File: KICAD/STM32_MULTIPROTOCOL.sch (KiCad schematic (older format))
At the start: 77 parts, among them T1 TestPoint, T10 TestPoint, T11 TestPoint, T12 TestPoint, T13 TestPoint, T14 TestPoint, T2 TestPoint, T3 TestPoint, T4 TestPoint, T5 TestPoint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

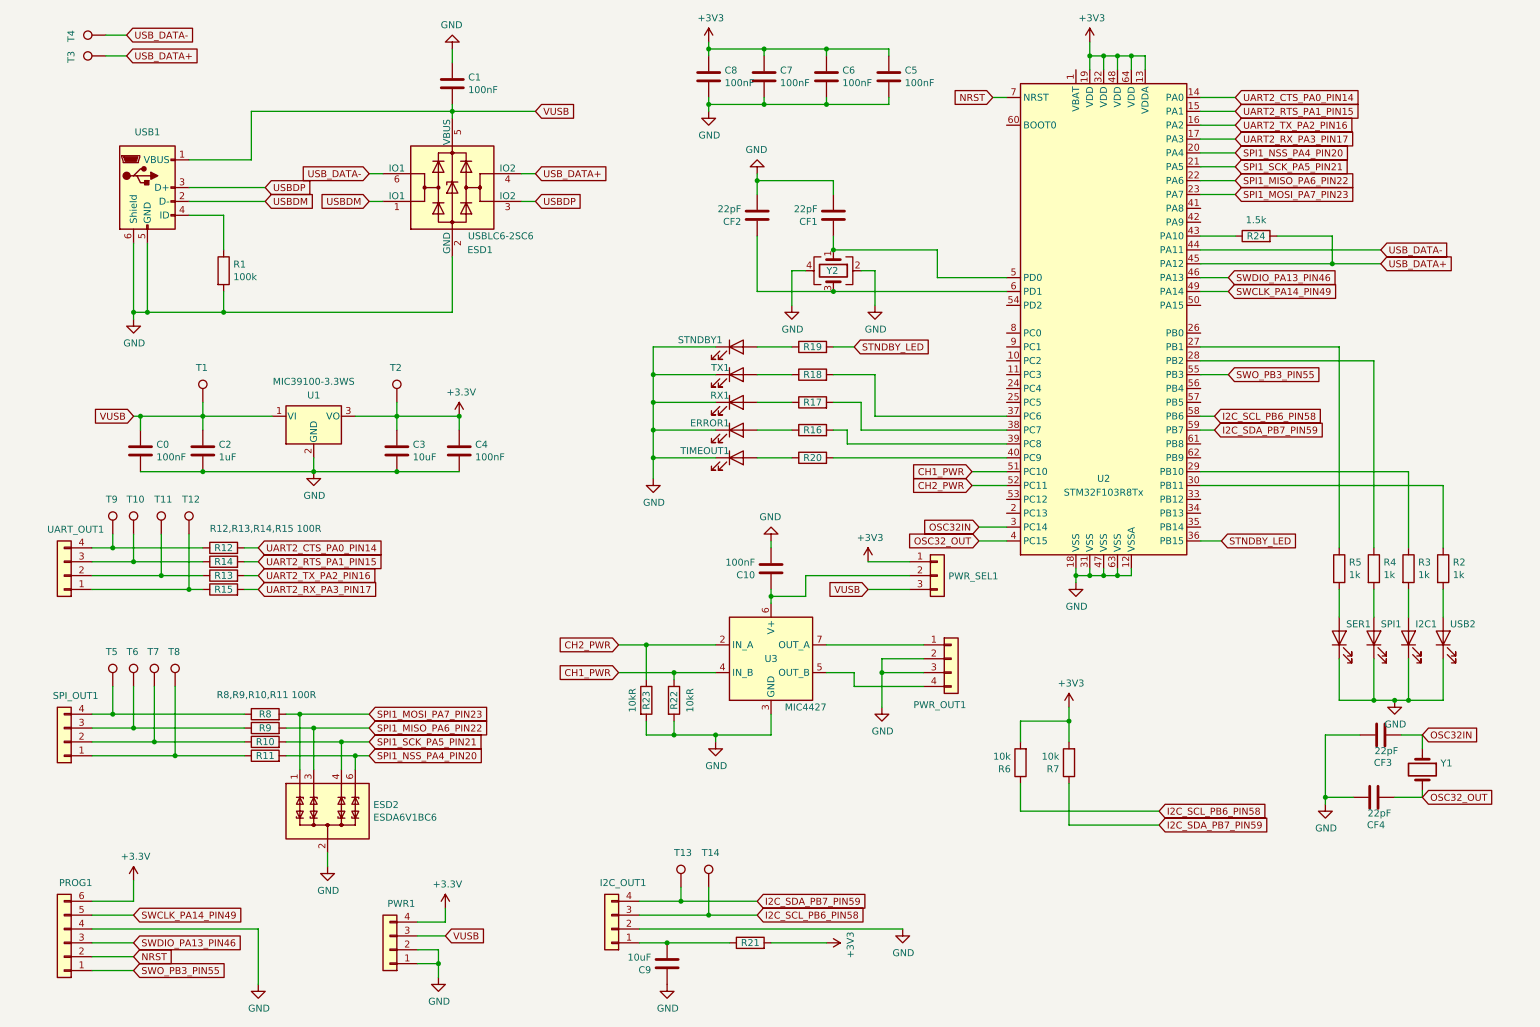
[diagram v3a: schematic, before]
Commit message: added pcb revision 2, fixed firmware project for cloners
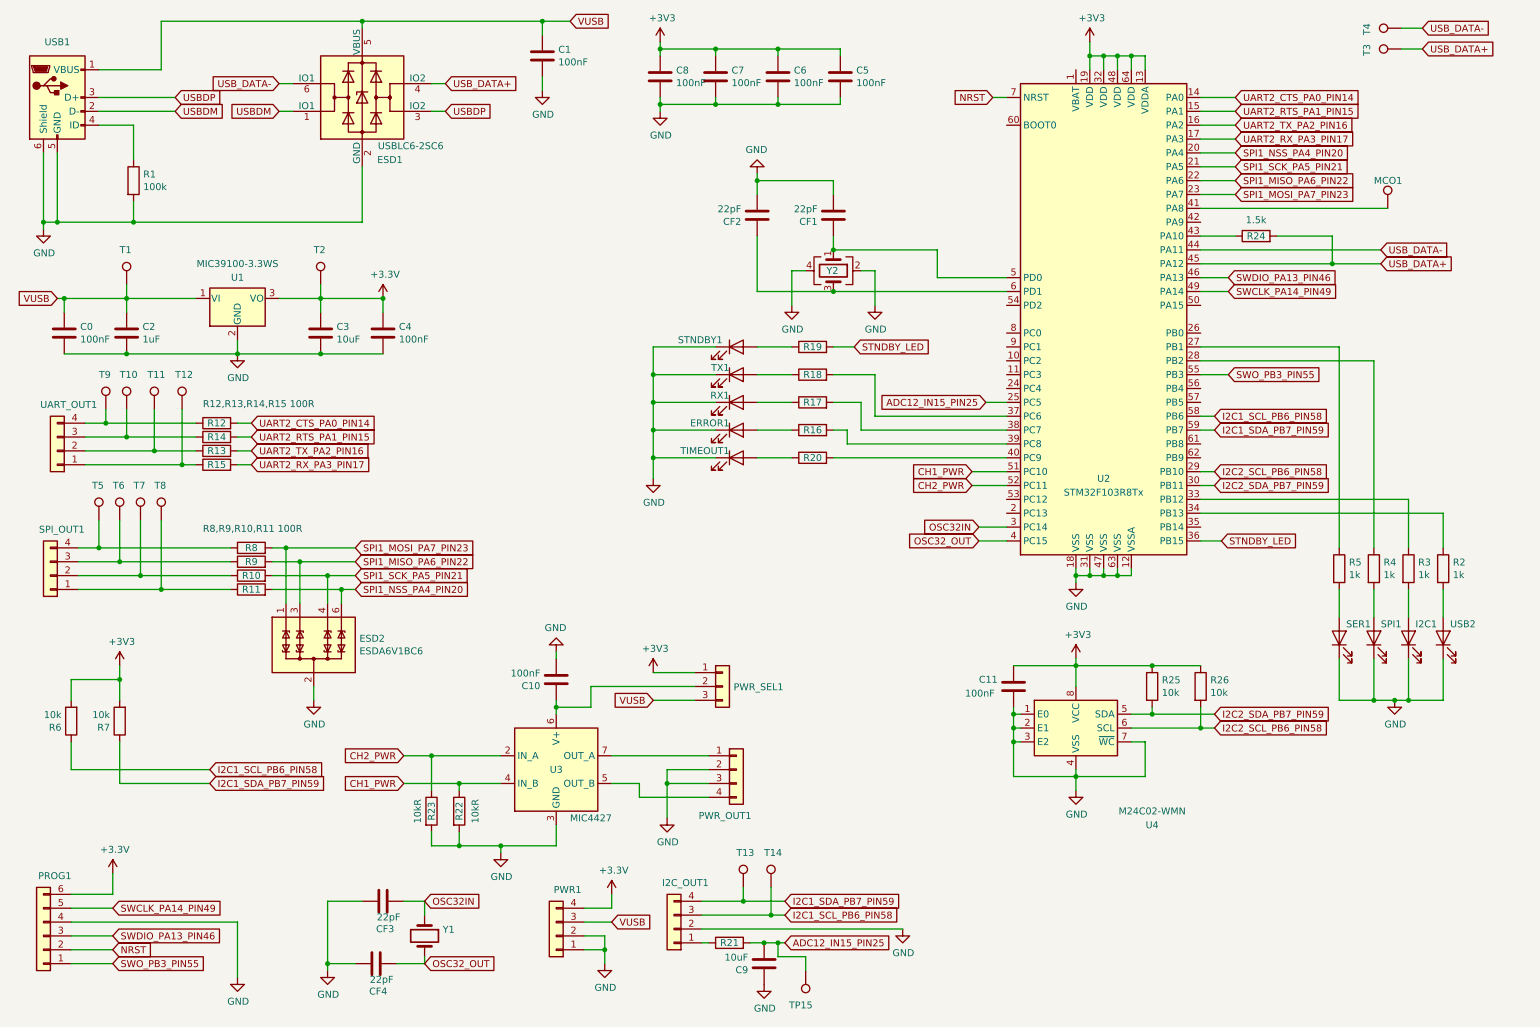
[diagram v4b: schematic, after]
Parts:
- added C11: 100nF, Resistor_SMD:R_0805_2012Metric_Pad1.15x1.40mm_HandSolder, symbol Device:C
- added MCO1: TestPoint, TestPoint:TestPoint_Pad_D1.0mm, symbol Connector:TestPoint
- added R25, R26: 10k, Resistor_SMD:R_0805_2012Metric_Pad1.15x1.40mm_HandSolder, symbol Device:R
- added TP15: TestPoint, TestPoint:TestPoint_Pad_D1.5mm, symbol Connector:TestPoint
- added U4: M24C02-WMN, Package_SO:SOIC-8_3.9x4.9mm_P1.27mm, symbol Memory_EEPROM:M24C02-WMN
- T10, T11, T12, T13, T14, T5, T6, T7, T8, T9: footprint TestPoint:TestPoint_Pad_D1.0mm -> TestPoint:TestPoint_Pad_D1.5mm
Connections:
- net +3V3: now also C11.1, R25.1, R26.1, U4.8 (VCC); no longer R21.2
- net GND: now also C1.2, C11.2, U4.1 (E0), U4.2 (E1), U4.3 (E2), U4.4 (VSS), U4.7 (~WC); no longer C1.1
- net VUSB: now also C1.1; no longer C1.2
- net ADC12_IN15_PIN25: now reaches U2.25 (PC5)
- net ADC12_IN15_PIN25: now also C9.2, R21.2, TP15.1
- net at R3.1: now also U2.33 (PB12); no longer U2.29 (PB10)
- net at R2.1: now also U2.34 (PB13); no longer U2.30 (PB11)
- net at U2.41 (PA8): now also MCO1.1
- net at I2C_OUT1.1 (Pin_1), R21.1: no longer C9.2
- net I2C_SCL_PB6_PIN58 renamed I2C1_SCL_PB6_PIN58
- net I2C_SDA_PB7_PIN59 renamed I2C1_SDA_PB7_PIN59
- new net I2C2_SCL_PB6_PIN58: R26.2, U2.29 (PB10), U4.6 (SCL)
- new net I2C2_SDA_PB7_PIN59: R25.2, U2.30 (PB11), U4.5 (SDA)
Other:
- moved on the sheet: C0, C1, C10, C2, C3, C4, C5, C6, C7, C8, C9, CF3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

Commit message: added rev 2 BOM, added driver for onboard 24C64 eeprom, improved app_usb
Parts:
- U4: value M24C02-WMN -> 24C64
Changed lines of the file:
@@
 U 1 1 61F132DF
 P 8100 5700
-F 0 "U4" H 8650 5000 50  0000 C CNN
-F 1 "M24C02-WMN" H 8650 5100 50  0000 C CNN
+F 0 "U4" H 7950 6000 50  0000 C CNN
+F 1 "24C64" H 8400 5250 50  0000 C CNN
 F 2 "Package_SO:SOIC-8_3.9x4.9mm_P1.27mm" H 8100 6050 50  0001 C CNN
 F 3 "http://www.st.com/content/ccc/resource/technical/document/datasheet/b0/d8/50/40/5a/85/49/6f/DM00071904.pdf/files/DM00071904.pdf/jcr:content/translations/en.DM00071904.pdf" H 8150 5200 50  0001 C CNN
